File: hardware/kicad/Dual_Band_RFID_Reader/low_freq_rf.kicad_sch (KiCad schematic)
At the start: 22 parts, among them U2 LM393, U3 LM324

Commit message: First pass at HF and LF schematics
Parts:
- C1, C2, C3, C4, C5, C6: symbol pspice:CAP -> Device:C
- D1: symbol pspice:DIODE -> Device:D
- R14: renamed from 56Ω; value R -> 56Ω
- gave numbers to parts that had none: 1
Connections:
- net at C4.2, C5.1, R9.1: now also D1.2 (A); no longer D1.1 (K)
- net at C6.1, L1.1: now also D1.1 (K); no longer D1.2 (A)
- net RX renamed LF_RF_RX
- net TX renamed LF_RF_TX
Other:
- moved on the sheet: L1, Q1, R1, R10, R14, R2, R3, R4, R5, R6, R7, R8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

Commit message: move sheet template to kicad project folder
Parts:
- C1, C2, C3, C4, C5, C6: footprint (none) -> Capacitor_SMD:C_0603_1608Metric_Pad1.08x0.95mm_HandSolder
- R1, R10, R14, R2, R3, R4, R5, R6, R7, R8, R9: footprint (none) -> Resistor_SMD:R_0603_1608Metric_Pad0.98x0.95mm_HandSolder

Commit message: adding Mousa's board work to branch
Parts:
- D1: footprint (none) -> ZenerDiodes:DIOAD829W49L456D191
- U2: footprint (none) -> DualComparator_LM393:SO08
- U3: footprint (none) -> GPOPAmp_LM324:SOIC127P600X175-14N
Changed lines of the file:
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@@
       (effects (font (size 1.27 1.27)))
     )
-    (property "Footprint" "" (id 2) (at 60.96 101.6 0)
+    (property "Footprint" "DualComparator_LM393:SO08" (id 2) (at 60.96 101.6 0)
       (effects (font (size 1.27 1.27)) hide)
     )
@@
       (effects (font (size 1.27 1.27)))
     )
-    (property "Footprint" "" (id 2) (at 231.14 96.52 0)
+    (property "Footprint" "ZenerDiodes:DIOAD829W49L456D191" (id 2) (at 231.14 96.52 0)
       (effects (font (size 1.27 1.27)) hide)
     )
@@
       (effects (font (size 1.27 1.27)))
     )
-    (property "Footprint" "" (id 2) (at 109.22 96.52 0)
+    (property "Footprint" "GPOPAmp_LM324:SOIC127P600X175-14N" (id 2) (at 109.22 96.52 0)
       (effects (font (size 1.27 1.27)) hide)
     )

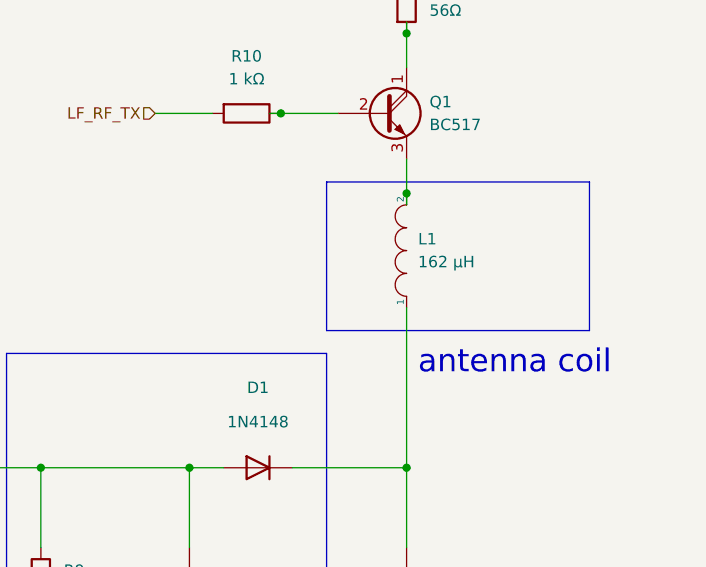
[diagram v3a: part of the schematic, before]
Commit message: Board Layout WIP
* Added correct footprint for the components that were
  producing errors
* added HF antenna trace on board periphery
* added pads for the LF antenna coil to be connected later
* corrected all the DRC errors
* completed HF layout
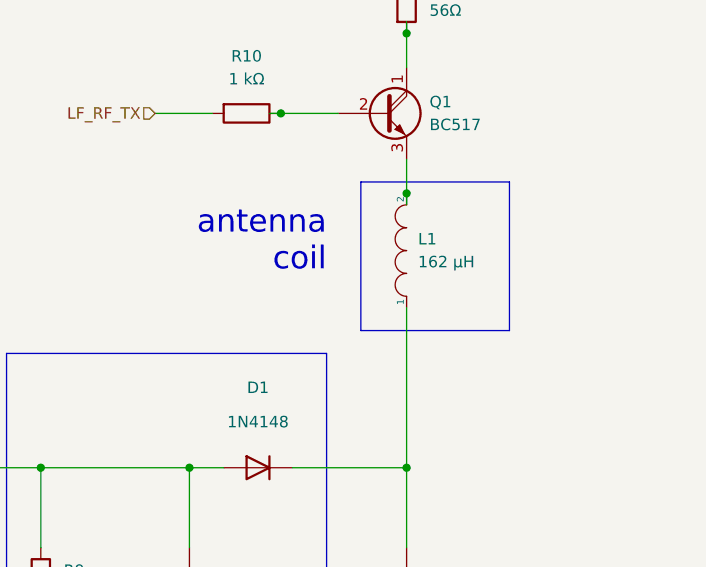
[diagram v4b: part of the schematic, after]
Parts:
- D1: footprint ZenerDiodes:DIOAD829W49L456D191 -> Diode_SMD:D_SOD-123
- L1: footprint (none) -> Capstone Footprint Lib:LF Antenna Pads
- Q1: footprint Package_TO_SOT_THT:TO-92_Inline -> Package_TO_SOT_SMD:SOT-223; Digi-Key URL (none) -> https://www.digikey.com/en/products/detail/onsemi/SPZT2222A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; Digi-Key part number (none) -> SPZT2222AT1GO; datasheet URL (none) -> https://www.onsemi.com/pdf/datasheet/pzt2222at1-d.pdf
- U2: footprint DualComparator_LM393:SO08 -> Package_SO:SOIC-8_3.9x4.9mm_P1.27mm; Digi-Key URL (none) -> https://www.digikey.com/en/products/detail/onsemi/LM393EDR2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; Digi-Key part number (none) -> LM393EDR2GO; datasheet URL (none) -> https://www.onsemi.com/pdf/datasheet/lm393-d.pdf
- U3: footprint GPOPAmp_LM324:SOIC127P600X175-14N -> Package_SO:SOIC-14_3.9x8.7mm_P1.27mm; Digi-Key URL (none) -> https://www.digikey.com/en/products/detail/onsemi/LM324DR2G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; Digi-Key part number (none) -> LM324DR2GO
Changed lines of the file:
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@@
     (stroke (width 0) (type default))
   )
-  (polyline (pts (xy 238.76 64.77) (xy 238.76 81.28))
-    (stroke (width 0) (type default))
-  )
-  (polyline (pts (xy 238.76 64.77) (xy 267.97 64.77))
-    (stroke (width 0) (type default))
-  )
-  (polyline (pts (xy 267.97 64.77) (xy 267.97 81.28))
-    (stroke (width 0) (type default))
-  )
-  (polyline (pts (xy 267.97 81.28) (xy 238.76 81.28))
+  (polyline (pts (xy 242.57 64.77) (xy 242.57 81.28))
+    (stroke (width 0) (type default))
+  )
+  (polyline (pts (xy 242.57 64.77) (xy 259.08 64.77))
+    (stroke (width 0) (type default))
+  )
+  (polyline (pts (xy 259.08 64.77) (xy 259.08 81.28))
+    (stroke (width 0) (type default))
+  )
+  (polyline (pts (xy 259.08 81.28) (xy 242.57 81.28))
     (stroke (width 0) (type default))
   )
@@
     (effects (font (size 2.54 2.54)) (justify left bottom))
   )
-  (text "antenna coil" (at 248.92 86.36 0)
-    (effects (font (size 2.54 2.54)) (justify left bottom))
+  (text "antenna\ncoil" (at 238.76 74.93 0)
+    (effects (font (size 2.54 2.54)) (justify right bottom))
   )
   (text "envelope detector" (at 204.47 133.35 0)
@@
       (effects (font (size 1.27 1.27)))
     )
-    (property "Footprint" "DualComparator_LM393:SO08" (id 2) (at 60.96 101.6 0)
-      (effects (font (size 1.27 1.27)) hide)
-    )
-    (property "Datasheet" "http://www.ti.com/lit/ds/symlink/lm393.pdf" (id 3) (at 60.96 101.6 0)
+    (property "Footprint" "Package_SO:SOIC-8_3.9x4.9mm_P1.27mm" (id 2) (at 60.96 101.6 0)
+      (effects (font (size 1.27 1.27)) hide)
+    )
+    (property "Datasheet" "https://www.onsemi.com/pdf/datasheet/lm393-d.pdf" (id 3) (at 60.96 101.6 0)
+      (effects (font (size 1.27 1.27)) hide)
+    )
+    (property "Digi-Key part number" "LM393EDR2GO" (id 4) (at 60.96 101.6 0)
+      (effects (font (size 1.27 1.27)) hide)
+    )
+    (property "Digi-Key URL" "https://www.digikey.com/en/products/detail/onsemi/LM393EDR2G/7220419" (id 5) (at 60.96 101.6 0)
+      (effects (font (size 1.27 1.27)) hide)
+    )
+    (property "datasheet URL" "https://www.onsemi.com/pdf/datasheet/lm393-d.pdf" (id 6) (at 60.96 101.6 0)
       (effects (font (size 1.27 1.27)) hide)
     )
@@
       (effects (font (size 1.27 1.27)))
     )
-    (property "Footprint" "ZenerDiodes:DIOAD829W49L456D191" (id 2) (at 231.14 96.52 0)
+    (property "Footprint" "Diode_SMD:D_SOD-123" (id 2) (at 231.14 96.52 0)
       (effects (font (size 1.27 1.27)) hide)
     )
@@
       (effects (font (size 1.27 1.27)) (justify right))
     )
-    (property "Footprint" "" (id 2) (at 247.65 72.39 0)
+    (property "Footprint" "Capstone Footprint Lib:LF Antenna Pads" (id 2) (at 247.65 72.39 0)
       (effects (font (size 1.27 1.27)) hide)
     )
@@
       (effects (font (size 1.27 1.27)))
     )
-    (property "Footprint" "GPOPAmp_LM324:SOIC127P600X175-14N" (id 2) (at 109.22 96.52 0)
-      (effects (font (size 1.27 1.27)) hide)
-    )
-    (property "Datasheet" "http://www.ti.com/lit/ds/symlink/lm2902-n.pdf" (id 3) (at 106.68 93.98 0)
+    (property "Footprint" "Package_SO:SOIC-14_3.9x8.7mm_P1.27mm" (id 2) (at 109.22 96.52 0)
+      (effects (font (size 1.27 1.27)) hide)
+    )
+    (property "Datasheet" "https://www.onsemi.com/pdf/datasheet/lm324-d.pdf" (id 3) (at 106.68 93.98 0)
+      (effects (font (size 1.27 1.27)) hide)
+    )
+    (property "Digi-Key part number" "LM324DR2GO" (id 4) (at 107.95 99.06 0)
+      (effects (font (size 1.27 1.27)) hide)
+    )
+    (property "Digi-Key URL" "https://www.digikey.com/en/products/detail/onsemi/LM324DR2G/918511" (id 5) (at 107.95 99.06 0)
       (effects (font (size 1.27 1.27)) hide)
     )
@@
       (effects (font (size 1.27 1.27)) (justify left))
     )
-    (property "Footprint" "Package_TO_SOT_THT:TO-92_Inline" (id 2) (at 250.19 59.055 0)
+    (property "Footprint" "Package_TO_SOT_SMD:SOT-223" (id 2) (at 250.19 59.055 0)
       (effects (font (size 1.27 1.27) italic) (justify left) hide)
     )
-    (property "Datasheet" "https://www.onsemi.com/pub/Collateral/BC517-D74Z-D.PDF" (id 3) (at 245.11 57.15 0)
+    (property "Datasheet" "" (id 3) (at 245.11 57.15 0)
       (effects (font (size 1.27 1.27)) (justify left) hide)
     )
-    (pin "1")
+    (property "Digi-Key part number" "SPZT2222AT1GO" (id 4) (at 245.11 57.15 0)
+      (effects (font (size 1.27 1.27)) hide)
+    )
+    (property "Digi-Key URL" "https://www.digikey.com/en/products/detail/onsemi/SPZT2222AT1G/3062863" (id 5) (at 245.11 57.15 0)
+      (effects (font (size 1.27 1.27)) hide)
+    )
+    (property "datasheet URL" "https://www.onsemi.com/pdf/datasheet/pzt2222at1-d.pdf" (id 6) (at 245.11 57.15 0)
+      (effects (font (size 1.27 1.27)) hide)
+    )
+    (pin "1")

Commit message: Updates traces
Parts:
- D1: footprint Diode_SMD:D_SOD-123 -> ZenerDiodes:DIOAD829W49L456D191
- L1: footprint Capstone Footprint Lib:LF Antenna Pads -> (none)
- Q1: footprint Package_TO_SOT_SMD:SOT-223 -> Package_TO_SOT_THT:TO-92_Inline; Digi-Key URL https://www.digikey.com/en/products/detail/onsemi/SPZT2222A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 -> (none); Digi-Key part number SPZT2222AT1GO -> (none); datasheet URL https://www.onsemi.com/pdf/datasheet/pzt2222at1-d.pdf -> (none)
- U2: footprint Package_SO:SOIC-8_3.9x4.9mm_P1.27mm -> DualComparator_LM393:SO08; Digi-Key URL https://www.digikey.com/en/products/detail/onsemi/LM393EDR2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 -> (none); Digi-Key part number LM393EDR2GO -> (none); datasheet URL https://www.onsemi.com/pdf/datasheet/lm393-d.pdf -> (none)
- U3: footprint Package_SO:SOIC-14_3.9x8.7mm_P1.27mm -> GPOPAmp_LM324:SOIC127P600X175-14N; Digi-Key URL https://www.digikey.com/en/products/detail/onsemi/LM324DR2G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 -> (none); Digi-Key part number LM324DR2GO -> (none)
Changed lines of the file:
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@@
   (junction (at 41.91 101.6) (diameter 0) (color 0 0 0 0)
   )
-  (junction (at 233.68 57.15) (diameter 0) (color 0 0 0 0)
-  )
   (junction (at 247.65 96.52) (diameter 0) (color 0 0 0 0)
   )
@@
   (junction (at 76.2 130.81) (diameter 0) (color 0 0 0 0)
   )
-  (junction (at 247.65 66.04) (diameter 0) (color 0 0 0 0)
-  )
   (junction (at 223.52 96.52) (diameter 0) (color 0 0 0 0)
   )
@@
   (junction (at 119.38 111.76) (diameter 0) (color 0 0 0 0)
   )
-  (junction (at 247.65 40.64) (diameter 0) (color 0 0 0 0)
-  )
   (junction (at 207.01 96.52) (diameter 0) (color 0 0 0 0)
   )
-  (junction (at 247.65 127) (diameter 0) (color 0 0 0 0)
-  )
-  (junction (at 247.65 48.26) (diameter 0) (color 0 0 0 0)
-  )
   (junction (at 247.65 121.92) (diameter 0) (color 0 0 0 0)
   )
@@
     (stroke (width 0) (type default))
   )
-  (wire (pts (xy 232.41 57.15) (xy 233.68 57.15))
-    (stroke (width 0) (type default))
-  )
   (wire (pts (xy 219.71 57.15) (xy 226.06 57.15))
     (stroke (width 0) (type default))
@@
     (stroke (width 0) (type default))
   )
-  (wire (pts (xy 247.65 46.99) (xy 247.65 48.26))
-    (stroke (width 0) (type default))
-  )
   (wire (pts (xy 207.01 96.52) (xy 207.01 105.41))
     (stroke (width 0) (type default))
@@
     (stroke (width 0) (type default))
   )
-  (wire (pts (xy 247.65 40.64) (xy 247.65 41.91))
-    (stroke (width 0) (type default))
-  )
   (wire (pts (xy 207.01 113.03) (xy 207.01 121.92))
     (stroke (width 0) (type default))
@@
     (stroke (width 0) (type default))
   )
-  (polyline (pts (xy 242.57 64.77) (xy 242.57 81.28))
-    (stroke (width 0) (type default))
-  )
-  (polyline (pts (xy 242.57 64.77) (xy 259.08 64.77))
-    (stroke (width 0) (type default))
-  )
-  (polyline (pts (xy 259.08 64.77) (xy 259.08 81.28))
-    (stroke (width 0) (type default))
-  )
-  (polyline (pts (xy 259.08 81.28) (xy 242.57 81.28))
+  (polyline (pts (xy 238.76 64.77) (xy 238.76 81.28))
+    (stroke (width 0) (type default))
+  )
+  (polyline (pts (xy 238.76 64.77) (xy 267.97 64.77))
+    (stroke (width 0) (type default))
+  )
+  (polyline (pts (xy 267.97 64.77) (xy 267.97 81.28))
+    (stroke (width 0) (type default))
+  )
+  (polyline (pts (xy 267.97 81.28) (xy 238.76 81.28))
     (stroke (width 0) (type default))
   )
@@
     (stroke (width 0) (type default))
   )
-  (wire (pts (xy 247.65 127) (xy 247.65 128.27))
-    (stroke (width 0) (type default))
-  )
   (wire (pts (xy 233.68 57.15) (xy 240.03 57.15))
     (stroke (width 0) (type default))
@@
   )
   (wire (pts (xy 41.91 97.79) (xy 41.91 101.6))
-    (stroke (width 0) (type default))
-  )
-  (wire (pts (xy 247.65 66.04) (xy 247.65 67.31))
     (stroke (width 0) (type default))
   )
@@
     (effects (font (size 2.54 2.54)) (justify left bottom))
   )
-  (text "antenna\ncoil" (at 238.76 74.93 0)
-    (effects (font (size 2.54 2.54)) (justify right bottom))
+  (text "antenna coil" (at 248.92 86.36 0)
+    (effects (font (size 2.54 2.54)) (justify left bottom))
   )
   (text "envelope detector" (at 204.47 133.35 0)
@@
       (effects (font (size 1.27 1.27)))
     )
-    (property "Footprint" "Package_SO:SOIC-8_3.9x4.9mm_P1.27mm" (id 2) (at 60.96 101.6 0)
-      (effects (font (size 1.27 1.27)) hide)
-    )
-    (property "Datasheet" "https://www.onsemi.com/pdf/datasheet/lm393-d.pdf" (id 3) (at 60.96 101.6 0)
-      (effects (font (size 1.27 1.27)) hide)
-    )
-    (property "Digi-Key part number" "LM393EDR2GO" (id 4) (at 60.96 101.6 0)
-      (effects (font (size 1.27 1.27)) hide)
-    )
-    (property "Digi-Key URL" "https://www.digikey.com/en/products/detail/onsemi/LM393EDR2G/7220419" (id 5) (at 60.96 101.6 0)
-      (effects (font (size 1.27 1.27)) hide)
-    )
-    (property "datasheet URL" "https://www.onsemi.com/pdf/datasheet/lm393-d.pdf" (id 6) (at 60.96 101.6 0)
+    (property "Footprint" "DualComparator_LM393:SO08" (id 2) (at 60.96 101.6 0)
+      (effects (font (size 1.27 1.27)) hide)
+    )
+    (property "Datasheet" "http://www.ti.com/lit/ds/symlink/lm393.pdf" (id 3) (at 60.96 101.6 0)
       (effects (font (size 1.27 1.27)) hide)
     )
@@
     (pin "2")
     (pin "3")
+    (pin "5")
+    (pin "6")
+    (pin "7")
+    (pin "4")
+    (pin "8")
   )
   (symbol (lib_id "Device:D") (at 231.14 96.52 0) (mirror y) (unit 1)
@@
       (effects (font (size 1.27 1.27)))
     )
-    (property "Footprint" "Diode_SMD:D_SOD-123" (id 2) (at 231.14 96.52 0)
+    (property "Footprint" "ZenerDiodes:DIOAD829W49L456D191" (id 2) (at 231.14 96.52 0)
       (effects (font (size 1.27 1.27)) hide)
     )
@@
       (effects (font (size 1.27 1.27)) (justify right))
     )
-    (property "Footprint" "Capstone Footprint Lib:LF Antenna Pads" (id 2) (at 247.65 72.39 0)
+    (property "Footprint" "" (id 2) (at 247.65 72.39 0)
       (effects (font (size 1.27 1.27)) hide)
     )
@@
       (effects (font (size 1.27 1.27)))
     )
-    (property "Footprint" "Package_SO:SOIC-14_3.9x8.7mm_P1.27mm" (id 2) (at 109.22 96.52 0)
-      (effects (font (size 1.27 1.27)) hide)
-    )
-    (property "Datasheet" "https://www.onsemi.com/pdf/datasheet/lm324-d.pdf" (id 3) (at 106.68 93.98 0)
-      (effects (font (size 1.27 1.27)) hide)
-    )
-    (property "Digi-Key part number" "LM324DR2GO" (id 4) (at 107.95 99.06 0)
-      (effects (font (size 1.27 1.27)) hide)
-    )
-    (property "Digi-Key URL" "https://www.digikey.com/en/products/detail/onsemi/LM324DR2G/918511" (id 5) (at 107.95 99.06 0)
+    (property "Footprint" "GPOPAmp_LM324:SOIC127P600X175-14N" (id 2) (at 109.22 96.52 0)
+      (effects (font (size 1.27 1.27)) hide)
+    )
+    (property "Datasheet" "http://www.ti.com/lit/ds/symlink/lm2902-n.pdf" (id 3) (at 106.68 93.98 0)
       (effects (font (size 1.27 1.27)) hide)
     )
@@
     (pin "2")
     (pin "3")
+    (pin "5")
+    (pin "6")
+    (pin "7")
+    (pin "10")
+    (pin "8")
+    (pin "9")
+    (pin "12")
+    (pin "13")
+    (pin "14")
+    (pin "11")
+    (pin "4")
   )
   (symbol (lib_id "power:+3.3V") (at 76.2 115.57 0) (unit 1)
@@
       (effects (font (size 1.27 1.27)) (justify left))
     )
-    (property "Footprint" "Package_TO_SOT_SMD:SOT-223" (id 2) (at 250.19 59.055 0)
+    (property "Footprint" "Package_TO_SOT_THT:TO-92_Inline" (id 2) (at 250.19 59.055 0)
       (effects (font (size 1.27 1.27) italic) (justify left) hide)
     )
-    (property "Datasheet" "" (id 3) (at 245.11 57.15 0)
+    (property "Datasheet" "https://www.onsemi.com/pub/Collateral/BC517-D74Z-D.PDF" (id 3) (at 245.11 57.15 0)
       (effects (font (size 1.27 1.27)) (justify left) hide)
     )
-    (property "Digi-Key part number" "SPZT2222AT1GO" (id 4) (at 245.11 57.15 0)
-      (effects (font (size 1.27 1.27)) hide)
-    )
-    (property "Digi-Key URL" "https://www.digikey.com/en/products/detail/onsemi/SPZT2222AT1G/3062863" (id 5) (at 245.11 57.15 0)
-      (effects (font (size 1.27 1.27)) hide)
-    )
-    (property "datasheet URL" "https://www.onsemi.com/pdf/datasheet/pzt2222at1-d.pdf" (id 6) (at 245.11 57.15 0)
-      (effects (font (size 1.27 1.27)) hide)
-    )
-    (pin "1")
+    (pin "1")
